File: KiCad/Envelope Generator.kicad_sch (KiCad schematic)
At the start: 0 parts

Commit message: amplifier sch., general changes to oscillator sch.
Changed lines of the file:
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@@
 	(generator_version "10.0")
 	(paper "A4")
-	(hierarchical_label "Out"
+	(hierarchical_label "Amplifier Out"
 		(shape output)
 		(at 39.37 86.36 0)
 		(effects
 			(font
+				(size 1.27 1.27)
+			)
+			(justify left)
+		)
+	)
+	(hierarchical_label "Filter Out"
+		(shape output)
+		(at 43.18 107.95 0)
+		(effects
+			(font

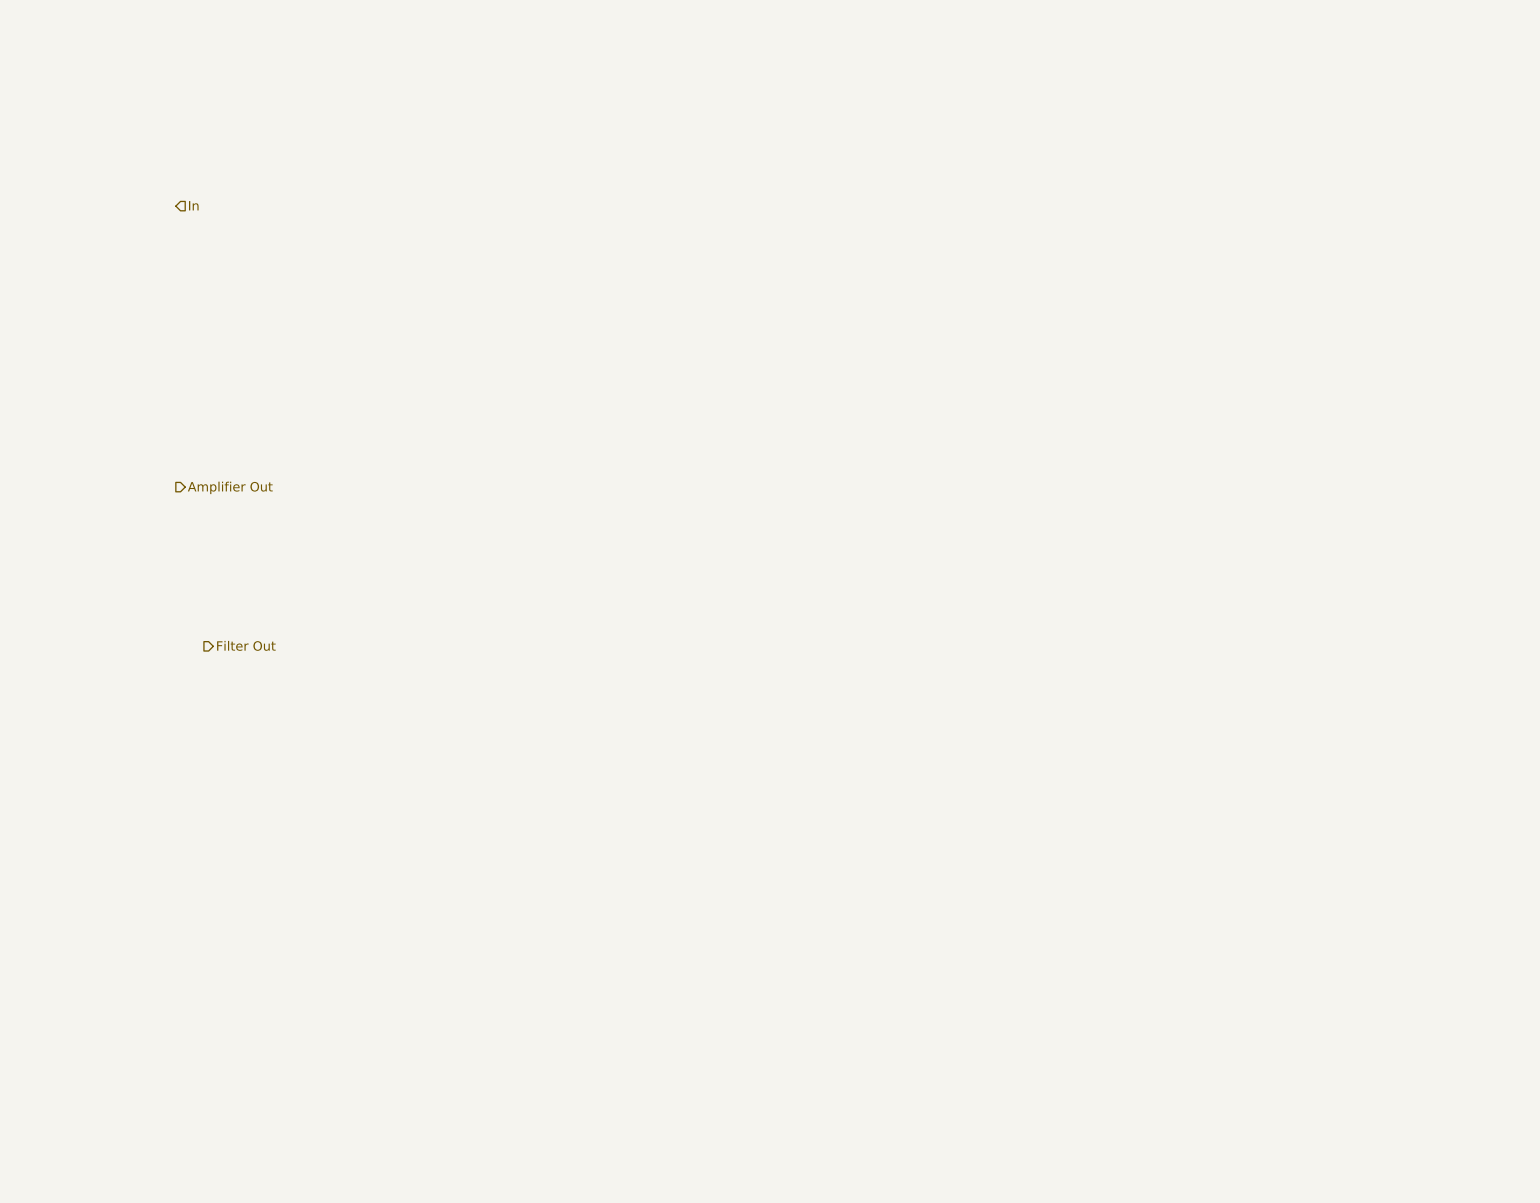
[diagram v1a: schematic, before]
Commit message: drafted a dual output envelope generator
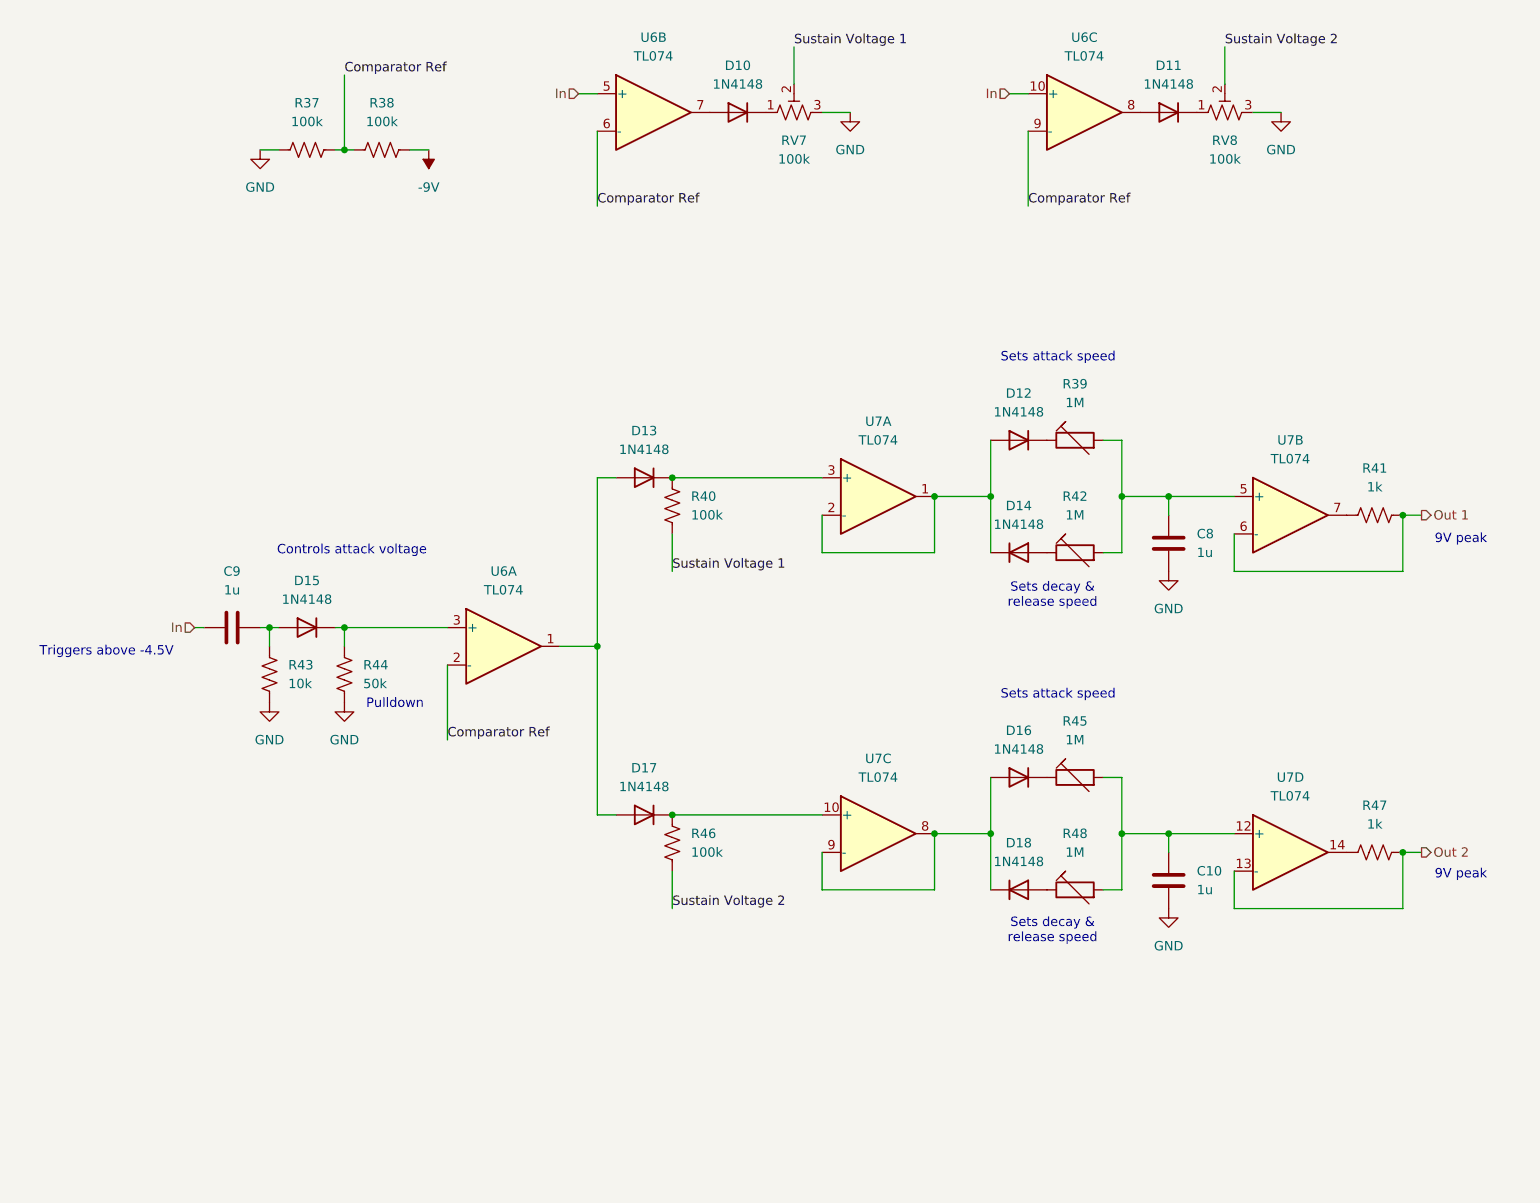
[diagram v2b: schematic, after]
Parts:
- added C10, C8, C9: 1u, symbol Device:C
- added D10, D11, D12, D13, D14, D15, D16, D17, D18: 1N4148, Diode_THT:D_DO-35_SOD27_P7.62mm_Horizontal, symbol Diode:1N4148
- added R37, R38, R40, R46: 100k, symbol Device:R_US
- added R39, R42, R45, R48: 1M, symbol Device:R_Trim
- added R41, R47: 1k, symbol Device:R_US
- added R43: 10k, symbol Device:R_US
- added R44: 50k, symbol Device:R_US
- added RV7, RV8: 100k, symbol Device:R_Potentiometer_Trim_US
- added U6, U7: TL074, symbol Amplifier_Operational:TL074
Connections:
- net In: now also C9.1, U6.10 (+), U6.5 (+)
- new net: C8.2, R39.2, R42.2, U7.5 (+)
- new net: D17.1 (K), R46.1, U7.10 (+)
- new net: D13.2 (A), D17.2 (A), U6.1
- new net: C10.2, R45.2, R48.2, U7.12 (+)
- new net: D11.2 (A), U6.8
- new net: R47.1, U7.14
- new net: D15.1 (K), R44.1, U6.3 (+)
- new net: D16.2 (A), D18.1 (K), U7.8, U7.9 (-)
- new net: D10.1 (K), RV7.1
- new net: D12.1 (K), R39.1
- new net: D12.2 (A), D14.1 (K), U7.1, U7.2 (-)
- new net: C9.2, D15.2 (A), R43.1
- new net: R41.1, U7.7
- new net: D14.2 (A), R42.1
- new net: D18.2 (A), R48.1
- new net: D16.1 (K), R45.1
- new net: D13.1 (K), R40.1, U7.3 (+)
- new net: D11.1 (K), RV8.1
- new net: D10.2 (A), U6.7
- new net -9V: R38.2
- new net Comparator Ref: R37.2, R38.1, U6.2 (-), U6.6 (-), U6.9 (-)
- new net GND: C10.1, C8.1, R37.1, R43.2, R44.2, RV7.3, RV8.3
- new net Out 1: R41.2, U7.6 (-)
- new net Out 2: R47.2, U7.13 (-)
- new net Sustain Voltage 1: R40.2, RV7.2
- new net Sustain Voltage 2: R46.2, RV8.2
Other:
- note added: "9V peak"
- note added: "Controls attack voltage"
- note added: "Pulldown"
- note added: "Sets attack speed"
- note added: "Sets decay & release speed"
- note added: "Triggers above -4.5V"

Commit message: drafted envelope generator LTspice simulation
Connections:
- net Comparator Ref renamed Trigger Ref
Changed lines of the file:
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@@
 		)
 	)
-	(label "Comparator Ref"
+	(label "Trigger Ref"
 		(at 76.2 120.65 0)
 		(effects
@@
 		)
 	)
-	(label "Comparator Ref"
+	(label "Trigger Ref"
 		(at 62.23 30.48 0)
 		(effects
@@
 		)
 	)
-	(label "Comparator Ref"
+	(label "Trigger Ref"
 		(at 96.52 48.26 0)
 		(effects
@@
 		)
 	)
-	(label "Comparator Ref"
+	(label "Trigger Ref"
 		(at 154.94 48.26 0)
 		(effects

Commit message: finalizing schematic
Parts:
- removed R39, R42, R45, R48: 1M, symbol Device:R_Trim
- removed RV7, RV8: 100k, symbol Device:R_Potentiometer_Trim_US
- added C10: C, symbol Device:C
- added D17: 1N4148, Diode_THT:D_DO-35_SOD27_P7.62mm_Horizontal, symbol Diode:1N4148
- added R46, R47, R48, R49, R52, R57, R58, R59, R63: R_US, symbol Device:R_US
- added R60: 50k, symbol Device:R_US
- added unit 4 of U7
- C8: renamed from C9; value 1u -> C
- R53: renamed from R43; value 10k -> R_US
- renumbered C10 to C11, C8 to C9, D15 to D13, D13 to D14, D14 to D15, D17 to D18, D18 to D19, R37 to R50, R38 to R51, R44 to R54, R40 to R55, R41 to R56, R46 to R61, R47 to R62, U6 to U7, U7 to U8
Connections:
- net GND: now also R47.2, R49.2, R59.2, R60.2
- net In: now also C10.1
- net Trigger Ref: now also U7.13 (-)
- net at C9.2, U8.5 (+): now also R52.2, R57.2
- net at D14.2 (A), U7.1: no longer D18.2 (A)
- net at C11.2, U8.12 (+): now also R58.2, R63.2
- net at D10.1 (K): now also R46.1
- net at D12.1 (K): now also R52.1
- net at D15.2 (A): now also R57.1
- net at D19.2 (A): now also R63.1
- net at D16.1 (K): now also R58.1
- net at D11.1 (K): now also R48.1
- net Out 1 renamed Out Filter
- net Out 2 renamed Out Amp
- net Sustain Voltage 1 renamed Sustain Voltage Filter
- net Sustain Voltage Filter: now also R46.2, R47.1
- net Sustain Voltage 2 renamed Sustain Voltage Amp
- net Sustain Voltage Amp: now also R48.2, R49.1
- new net: C10.2, D17.2 (A), R59.1
- new net: D18.2 (A), U7.14
- new net: D17.1 (K), R60.1, U7.12 (+)
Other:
- note removed: "9V peak"
- note removed: "Pulldown"
- moved on the sheet: C8, D13, R53, R54, U7A

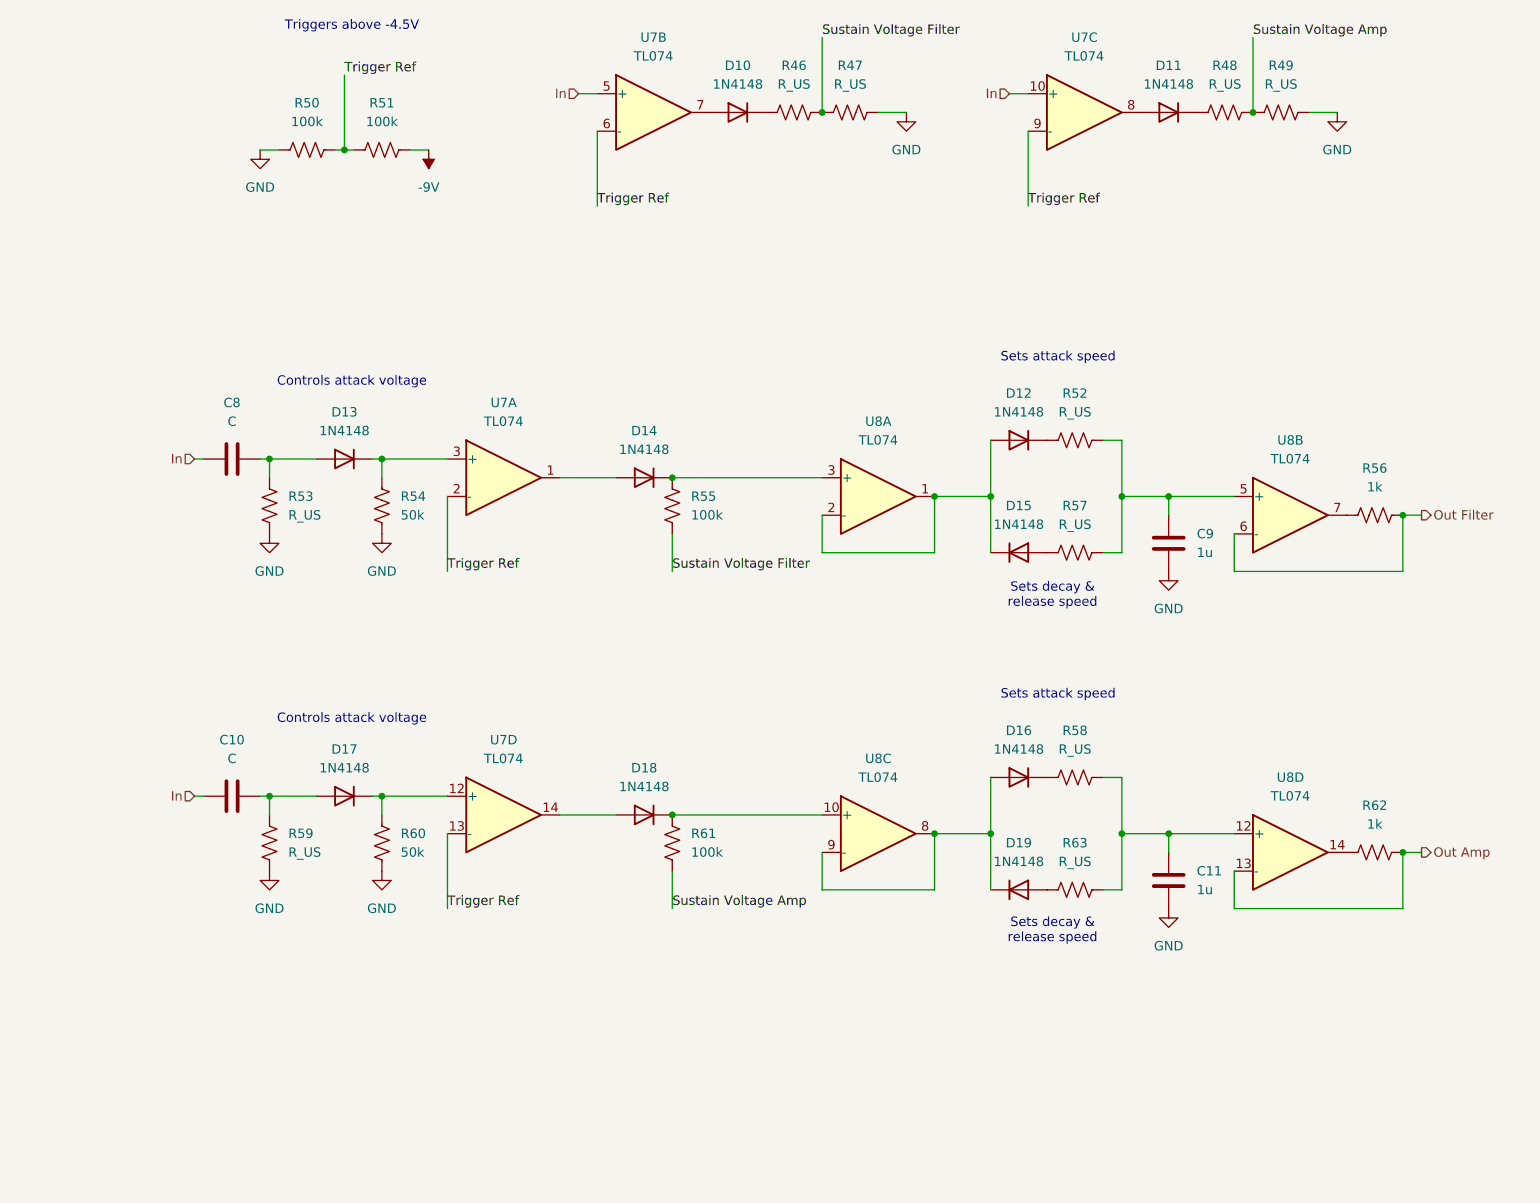
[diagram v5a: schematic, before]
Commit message: updated footprints
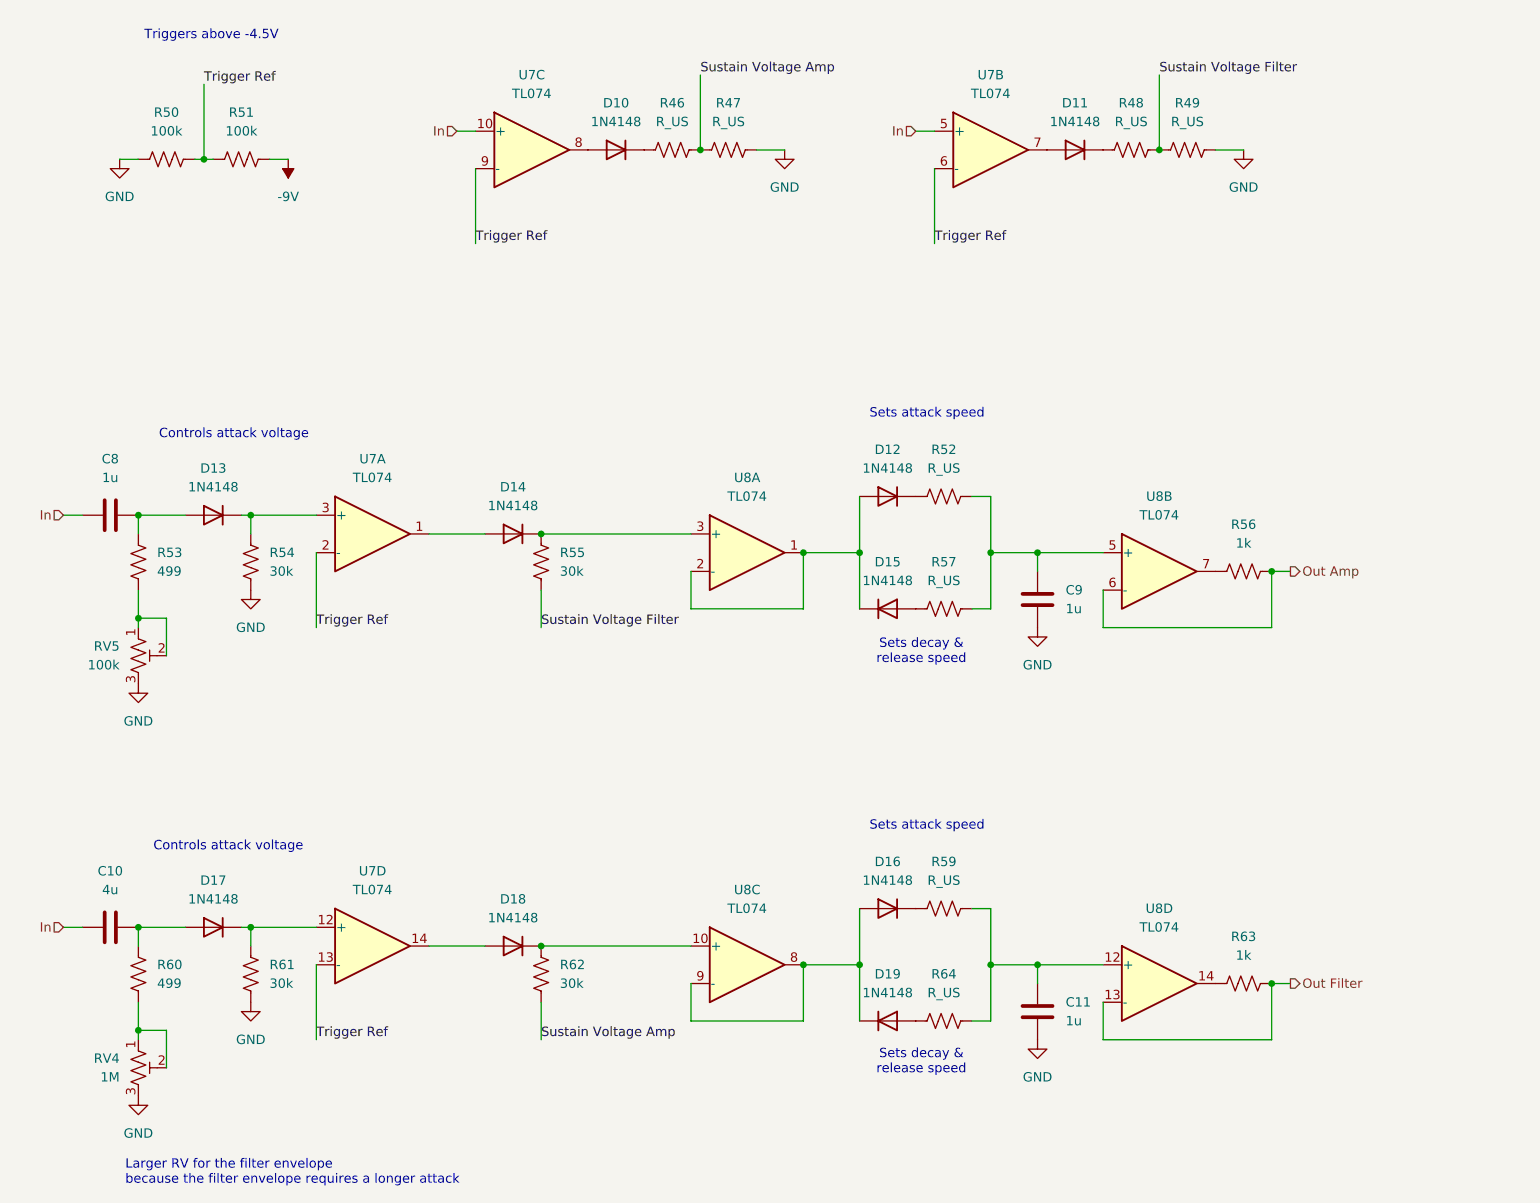
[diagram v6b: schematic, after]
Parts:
- added RV4: 1M, Potentiometer_THT:Potentiometer_Bourns_3296W_Vertical, symbol Device:R_Potentiometer_Trim_US
- added RV5: 100k, Potentiometer_THT:Potentiometer_Bourns_3296W_Vertical, symbol Device:R_Potentiometer_Trim_US
- C10: value C -> 4u; footprint (none) -> Capacitor_THT:C_Rect_L31.5mm_W20.0mm_P27.50mm_MKS4
- C11, C9: footprint (none) -> Capacitor_THT:C_Rect_L7.2mm_W4.5mm_P5.00mm
- C8: value C -> 1u; footprint (none) -> Capacitor_THT:C_Rect_L7.2mm_W4.5mm_P5.00mm
- R46: renamed from R48; footprint (none) -> Resistor_THT:R_Axial_DIN0207_L6.3mm_D2.5mm_P7.62mm_Horizontal
- R47: renamed from R49; footprint (none) -> Resistor_THT:R_Axial_DIN0207_L6.3mm_D2.5mm_P7.62mm_Horizontal
- R48: renamed from R46; footprint (none) -> Resistor_THT:R_Axial_DIN0207_L6.3mm_D2.5mm_P7.62mm_Horizontal
- R49: renamed from R47; footprint (none) -> Resistor_THT:R_Axial_DIN0207_L6.3mm_D2.5mm_P7.62mm_Horizontal
- R50, R51: footprint (none) -> Resistor_SMD:R_0201_0603Metric
- R52, R57: footprint (none) -> Resistor_THT:R_Axial_DIN0207_L6.3mm_D2.5mm_P7.62mm_Horizontal
- R53: value R_US -> 499; footprint (none) -> Resistor_THT:R_Axial_DIN0207_L6.3mm_D2.5mm_P7.62mm_Horizontal
- R54: value 50k -> 30k; footprint (none) -> Resistor_SMD:R_0201_0603Metric
- R55: value 100k -> 30k; footprint (none) -> Resistor_SMD:R_0201_0603Metric
- R56: footprint (none) -> Resistor_SMD:R_0402_1005Metric
- R59: renamed from R58; footprint (none) -> Resistor_THT:R_Axial_DIN0207_L6.3mm_D2.5mm_P7.62mm_Horizontal
- R60: renamed from R59; value R_US -> 499; footprint (none) -> Resistor_THT:R_Axial_DIN0207_L6.3mm_D2.5mm_P7.62mm_Horizontal
- R61: renamed from R60; value 50k -> 30k; footprint (none) -> Resistor_SMD:R_0201_0603Metric
- R62: renamed from R61; value 100k -> 30k; footprint (none) -> Resistor_SMD:R_0201_0603Metric
- R63: renamed from R62; footprint (none) -> Resistor_SMD:R_0402_1005Metric
- R64: renamed from R63; footprint (none) -> Resistor_THT:R_Axial_DIN0207_L6.3mm_D2.5mm_P7.62mm_Horizontal
- U7, U8: footprint (none) -> Package_DIP:DIP-14_W7.62mm
- renumbered D11 to D10, D10 to D11
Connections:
- net GND: now also RV4.3, RV5.3; no longer R53.2, R60.2
- net Out Amp: now also R56.2, U8.6 (-); no longer R63.2, U8.13 (-)
- net Out Filter: now also R63.2, U8.13 (-); no longer R56.2, U8.6 (-)
- new net: R53.2, RV5.1, RV5.2
- new net: R60.2, RV4.1, RV4.2
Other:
- note added: "Larger RV for the filter envelope because the filter envelope requires a longer attack"
- moved on the sheet: C10, C11, C8, C9, D10, D11, D12, D13, D14, D15, D16, D17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
